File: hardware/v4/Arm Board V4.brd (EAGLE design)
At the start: 108 x 50.8 mm, 29 parts, among them P1 STELLARIS-LAUNCHPADSTELLARIS-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, U1 SN74LS241DW, U2 XBEE-1B3

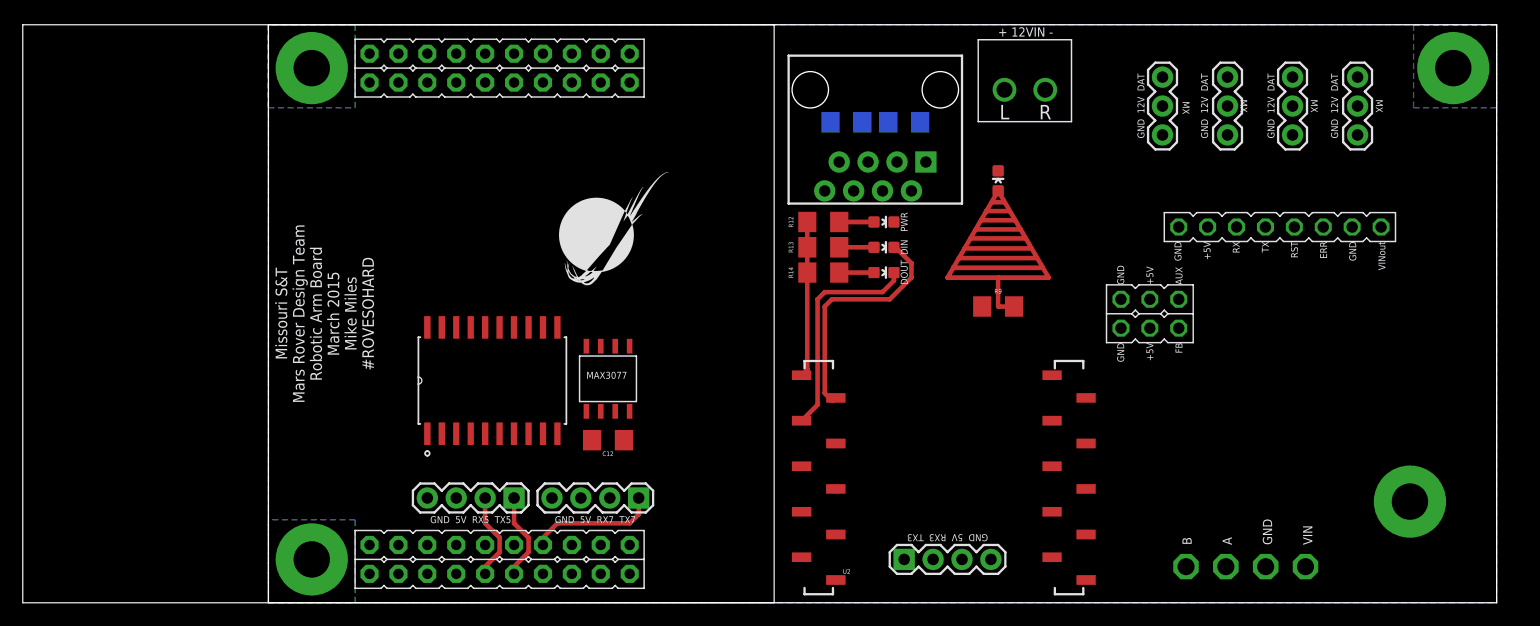
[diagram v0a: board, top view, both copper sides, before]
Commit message: reworking arm board
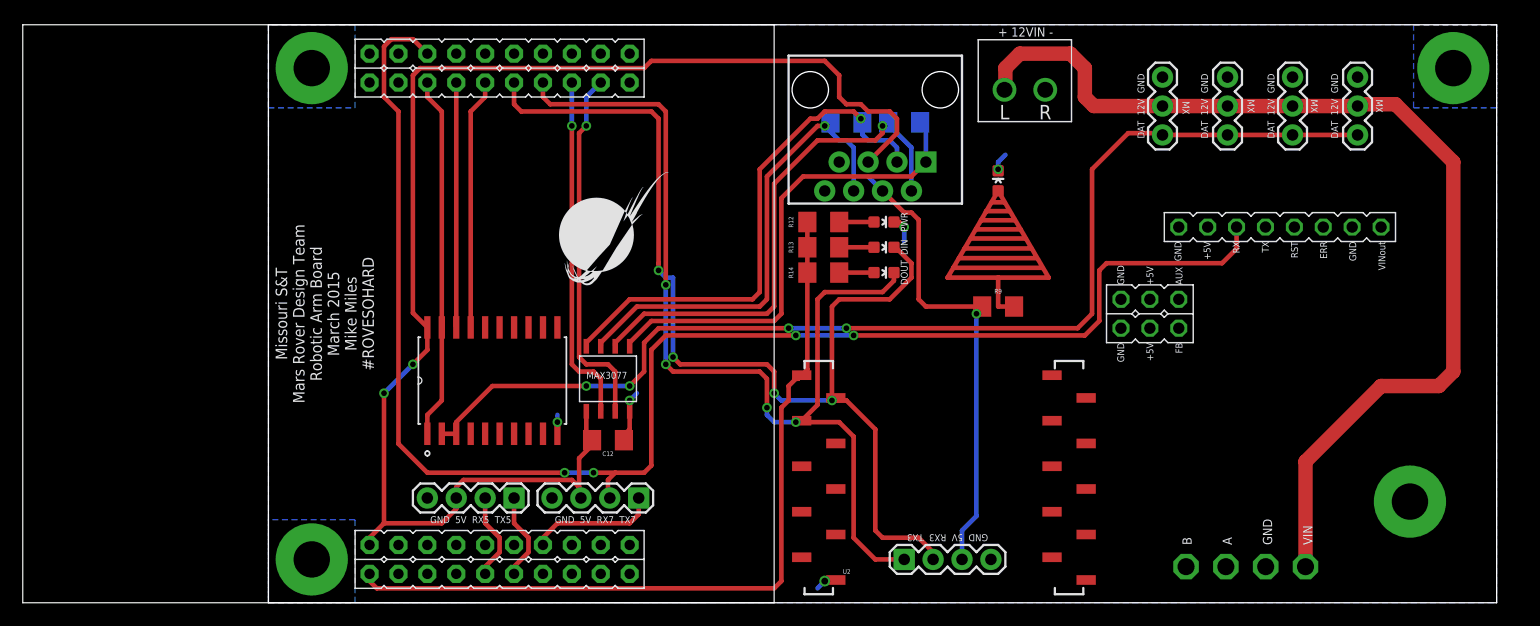
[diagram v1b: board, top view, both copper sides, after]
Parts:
- R9: value 1.5k -> 330
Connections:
- removed net 14.8V: JP10.2, JP11.2, JP12.2, JP9.2
- removed net VIN: R9.2
- net +12V: now also JP10.2, JP11.2, JP12.2, JP9.2
- net +5V: now also R9.2
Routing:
- net +5V: track 0.00 -> 165.3 mm, vias 0 -> 3
- net RX_7: track 0.00 -> 135.9 mm, vias 0 -> 4
- net DDATA_1: track 0.00 -> 101.0 mm, vias 0 -> 4
- net +12V: track 0.00 -> 91.3 mm
- net RX_3: track 21.0 -> 93.8 mm, vias 0 -> 4
- net TX_3: track 19.4 -> 89.4 mm, vias 0 -> 4
- net +3V3: track 13.7 -> 70.0 mm
- net N$1: track 0.00 -> 45.9 mm, vias 0 -> 1
- net N$3: track 0.00 -> 45.7 mm, vias 0 -> 1
- net N$5: track 0.00 -> 42.6 mm
- net N$2: track 0.00 -> 42.1 mm, vias 0 -> 1
- net TX_2: track 0.00 -> 32.1 mm, vias 0 -> 1
- net DC_1: track 0.00 -> 31.9 mm
- net RX_2: track 0.00 -> 30.7 mm, vias 0 -> 1
- net TX_1: track 0.00 -> 22.0 mm
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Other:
- board text added: "DAT 12V GND"
- board text removed: "GND 12V DAT"

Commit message: reworking arm board
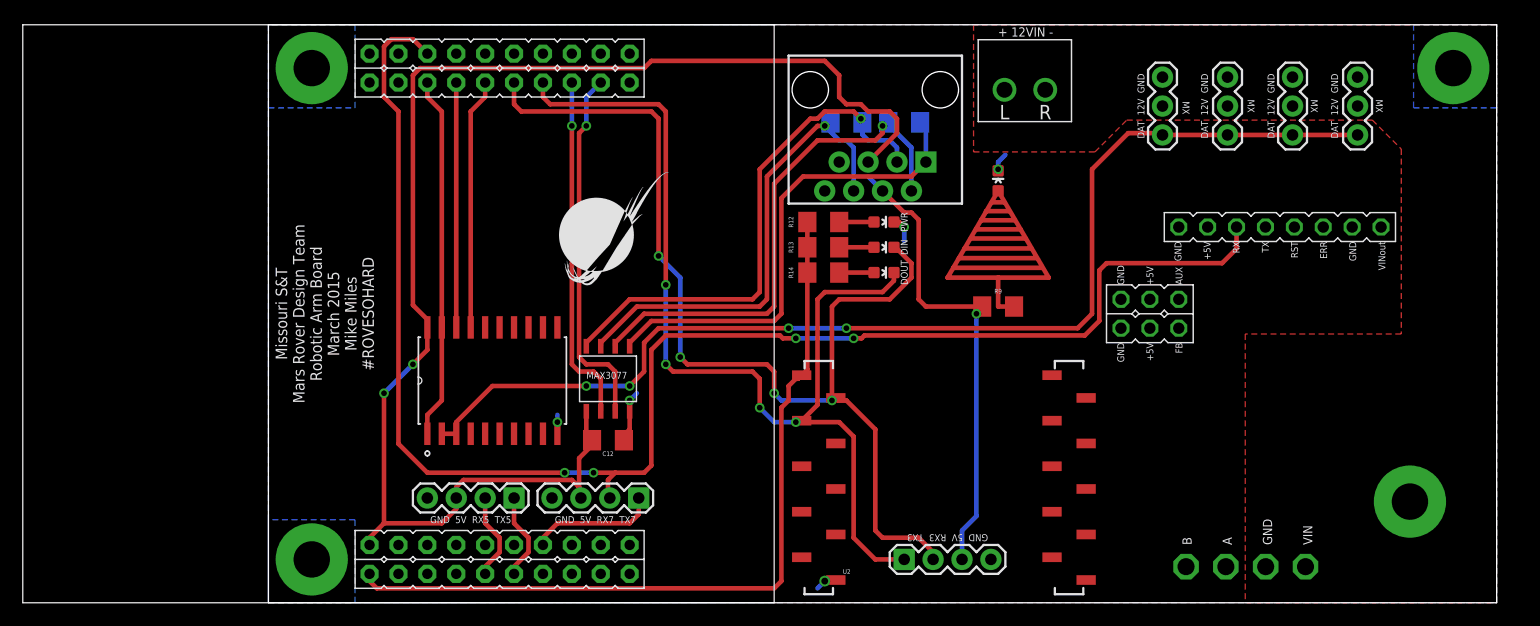
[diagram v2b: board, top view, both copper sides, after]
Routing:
- net +12V: track 91.3 -> 0.00 mm
- net RX_3: track 93.8 -> 93.0 mm
- added copper zone on layer 1, net +12V
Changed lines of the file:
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@@
 <setting verticaltext="up"/>
 </settings>
-<grid distance="0.05" unitdist="inch" unit="inch" style="lines" multiple="1" display="no" altdistance="0.025" altunitdist="inch" altunit="inch"/>
+<grid distance="0.01" unitdist="inch" unit="inch" style="lines" multiple="1" display="no" altdistance="0.0025" altunitdist="inch" altunit="inch"/>
 <layers>
 <layer number="1" name="Top" color="4" fill="1" visible="yes" active="yes"/>
@@
 <wire x1="33.02" y1="46.99" x2="13.335" y2="46.99" width="0.4064" layer="1"/>
 <wire x1="13.335" y1="46.99" x2="12.7" y2="46.355" width="0.4064" layer="1"/>
-<wire x1="12.7" y1="46.355" x2="12.7" y2="25.46985" width="0.4064" layer="1"/>
-<wire x1="12.7" y1="25.46985" x2="13.97" y2="24.19985" width="0.4064" layer="1"/>
 <wire x1="62.735" y1="26.035" x2="62.735" y2="25.905" width="0.4064" layer="1"/>
 <wire x1="62.735" y1="25.905" x2="62.23" y2="25.4" width="0.4064" layer="1"/>
@@
 <wire x1="62.23" y1="7.62" x2="60.96" y2="6.35" width="0.4064" layer="16"/>
 <wire x1="60.96" y1="6.35" x2="60.96" y2="3.81" width="0.4064" layer="16"/>
+<wire x1="13.97" y1="24.19985" x2="13.97" y2="24.892" width="0.4064" layer="1"/>
+<wire x1="13.97" y1="24.892" x2="12.7" y2="26.162" width="0.4064" layer="1"/>
+<wire x1="12.7" y1="26.162" x2="12.7" y2="46.355" width="0.4064" layer="1"/>
 <wire x1="52.705" y1="38.735" x2="52.705" y2="37.465" width="0" layer="19" extent="16-16"/>
 </signal>
@@
 <contactref element="U$7" pad="L"/>
 <contactref element="U$1" pad="VIN"/>
-<wire x1="91.149478125" y1="3.171971875" x2="91.149478125" y2="12.409478125" width="1.27" layer="1"/>
-<wire x1="91.149478125" y1="12.409478125" x2="97.79" y2="19.05" width="1.27" layer="1"/>
 <contactref element="JP9" pad="2"/>
 <contactref element="JP10" pad="2"/>
 <contactref element="JP11" pad="2"/>
 <contactref element="JP12" pad="2"/>
-<wire x1="97.79" y1="19.05" x2="102.87" y2="19.05" width="1.27" layer="1"/>
-<wire x1="102.87" y1="19.05" x2="104.14" y2="20.32" width="1.27" layer="1"/>
-<wire x1="104.14" y1="20.32" x2="104.14" y2="38.735" width="1.27" layer="1"/>
-<wire x1="104.14" y1="38.735" x2="99.06" y2="43.815" width="1.27" layer="1"/>
-<wire x1="99.06" y1="43.815" x2="95.885" y2="43.815" width="1.27" layer="1"/>
-<wire x1="95.885" y1="43.815" x2="95.72625" y2="43.65625" width="1.27" layer="1"/>
-<wire x1="95.72625" y1="43.65625" x2="90.01125" y2="43.65625" width="1.27" layer="1"/>
-<wire x1="90.01125" y1="43.65625" x2="84.29625" y2="43.65625" width="1.27" layer="1"/>
-<wire x1="84.29625" y1="43.65625" x2="78.58125" y2="43.65625" width="1.27" layer="1"/>
-<wire x1="78.58125" y1="43.65625" x2="72.54875" y2="43.65625" width="1.27" layer="1"/>
-<wire x1="72.54875" y1="43.65625" x2="71.755" y2="44.45" width="1.27" layer="1"/>
-<wire x1="71.755" y1="44.45" x2="71.755" y2="46.99" width="1.27" layer="1"/>
-<wire x1="71.755" y1="46.99" x2="70.485" y2="48.26" width="1.27" layer="1"/>
-<wire x1="70.485" y1="48.26" x2="66.04" y2="48.26" width="1.27" layer="1"/>
-<wire x1="66.04" y1="48.26" x2="64.77" y2="46.99" width="1.27" layer="1"/>
-<wire x1="64.77" y1="46.99" x2="64.77" y2="45.1605" width="1.27" layer="1"/>
-<wire x1="64.77" y1="45.1605" x2="64.6945" y2="45.085" width="1.27" layer="1"/>
+<polygon width="0.4064" layer="1">
+<vertex x="107.95" y="0"/>
+<vertex x="107.95" y="50.8"/>
+<vertex x="61.976" y="50.8"/>
+<vertex x="61.976" y="39.624"/>
+<vertex x="72.644" y="39.624"/>
+<vertex x="75.438" y="42.418"/>
+<vertex x="97.028" y="42.418"/>
+<vertex x="99.568" y="39.878"/>
+<vertex x="99.568" y="23.622"/>
+<vertex x="85.852" y="23.622"/>
+<vertex x="85.852" y="0"/>
+</polygon>
 </signal>
 <signal name="RST">
@@
 <wire x1="50.8" y1="17.78" x2="50.09" y2="17.78" width="0.4064" layer="1"/>
 <wire x1="50.09" y1="17.78" x2="49.87" y2="18" width="0.4064" layer="1"/>
-<wire x1="35.56" y1="28.575" x2="35.56" y2="21.59" width="0.4064" layer="16"/>
-<via x="35.56" y="21.59" extent="1-16" drill="0.5"/>
-<wire x1="35.56" y1="21.59" x2="36.195" y2="20.955" width="0.4064" layer="1"/>
-<wire x1="36.195" y1="20.955" x2="43.815" y2="20.955" width="0.4064" layer="1"/>
+<via x="36.195" y="21.59" extent="1-16" drill="0.5"/>
+<wire x1="36.195" y1="21.59" x2="36.83" y2="20.955" width="0.4064" layer="1"/>
+<wire x1="36.83" y1="20.955" x2="43.815" y2="20.955" width="0.4064" layer="1"/>
 <wire x1="43.815" y1="20.955" x2="44.45" y2="20.32" width="0.4064" layer="1"/>
 <wire x1="44.45" y1="20.32" x2="44.45" y2="18.415" width="0.4064" layer="1"/>
@@
 <wire x1="22.225" y1="43.18" x2="33.655" y2="43.18" width="0.4064" layer="1"/>
 <wire x1="33.655" y1="43.18" x2="34.29" y2="42.545" width="0.4064" layer="1"/>
-<wire x1="34.29" y1="42.545" x2="34.29" y2="29.845" width="0.4064" layer="1"/>
-<wire x1="35.56" y1="28.575" x2="34.925" y2="28.575" width="0.4064" layer="16"/>
-<wire x1="34.925" y1="28.575" x2="34.29" y2="29.21" width="0.4064" layer="16"/>
-<via x="34.29" y="29.21" extent="1-16" drill="0.5"/>
-<wire x1="34.29" y1="29.21" x2="34.29" y2="29.845" width="0.4064" layer="1"/>
+<wire x1="34.29" y1="42.545" x2="34.29" y2="30.48" width="0.4064" layer="1"/>
+<via x="34.29" y="30.48" extent="1-16" drill="0.5"/>
+<wire x1="34.29" y1="30.48" x2="36.195" y2="28.575" width="0.4064" layer="16"/>
+<wire x1="36.195" y1="28.575" x2="36.195" y2="21.59" width="0.4064" layer="16"/>
 </signal>
 <signal name="TX_3">
@@
 <via x="34.925" y="27.94" extent="1-16" drill="0.5"/>
 <wire x1="34.925" y1="27.94" x2="34.925" y2="20.955" width="0.4064" layer="16"/>
-<via x="43.815" y="17.145" extent="1-16" drill="0.5"/>
-<wire x1="43.815" y1="17.145" x2="43.815" y2="16.51" width="0.4064" layer="16"/>
-<wire x1="43.815" y1="16.51" x2="44.45" y2="15.875" width="0.4064" layer="16"/>
 <wire x1="44.45" y1="15.875" x2="46.355" y2="15.875" width="0.4064" layer="16"/>
 <via x="46.355" y="15.875" extent="1-16" drill="0.5"/>
@@
 <via x="34.925" y="20.955" extent="1-16" drill="0.5"/>
 <wire x1="34.925" y1="20.955" x2="35.56" y2="20.32" width="0.4064" layer="1"/>
-<wire x1="35.56" y1="20.32" x2="43.18" y2="20.32" width="0.4064" layer="1"/>
-<wire x1="43.18" y1="20.32" x2="43.815" y2="19.685" width="0.4064" layer="1"/>
-<wire x1="43.815" y1="19.685" x2="43.815" y2="17.145" width="0.4064" layer="1"/>
 <wire x1="24.13" y1="45.72" x2="24.13" y2="44.45" width="0.4064" layer="1"/>
 <wire x1="24.13" y1="44.45" x2="24.765" y2="43.815" width="0.4064" layer="1"/>
@@
 <wire x1="34.29" y1="43.815" x2="34.925" y2="43.18" width="0.4064" layer="1"/>
 <wire x1="34.925" y1="43.18" x2="34.925" y2="27.94" width="0.4064" layer="1"/>
+<wire x1="35.56" y1="20.32" x2="42.545" y2="20.32" width="0.4064" layer="1"/>
+<wire x1="42.545" y1="20.32" x2="43.18" y2="19.685" width="0.4064" layer="1"/>
+<wire x1="43.18" y1="19.685" x2="43.18" y2="17.145" width="0.4064" layer="1"/>
+<via x="43.18" y="17.145" extent="1-16" drill="0.5"/>
+<wire x1="43.18" y1="17.145" x2="44.45" y2="15.875" width="0.4064" layer="16"/>
 </signal>
 <signal name="RX_1">
@@
 <contactref element="P1" pad="PC5"/>
 <contactref element="U1" pad="17"/>
-<wire x1="17.78" y1="24.19985" x2="17.78" y2="43.18" width="0.4064" layer="1"/>
 <wire x1="17.78" y1="43.18" x2="19.05" y2="44.45" width="0.4064" layer="1"/>
 <wire x1="19.05" y1="44.45" x2="19.05" y2="45.72" width="0.4064" layer="1"/>
+<wire x1="17.78" y1="24.19985" x2="17.78" y2="43.18" width="0.4064" layer="1"/>
 </signal>
 <signal name="RX_5">
@@
 <wire x1="73.025" y1="29.21" x2="73.025" y2="24.765" width="0.4064" layer="1"/>
 <wire x1="73.025" y1="24.765" x2="71.755" y2="23.495" width="0.4064" layer="1"/>
-<wire x1="71.755" y1="23.495" x2="51.435" y2="23.495" width="0.4064" layer="1"/>
-<via x="51.435" y="23.495" extent="1-16" drill="0.5"/>
+<wire x1="71.755" y1="23.495" x2="52.3875" y2="23.495" width="0.4064" layer="1"/>
+<wire x1="52.3875" y1="23.495" x2="52.1335" y2="23.241" width="0.4064" layer="1"/>
+<wire x1="52.1335" y1="23.241" x2="51.435" y2="23.241" width="0.4064" layer="1"/>
+<via x="51.435" y="23.241" extent="1-16" drill="0.5"/>
 <wire x1="34.925" y1="23.495" x2="33.655" y2="22.225" width="0.4064" layer="1"/>
 <wire x1="33.655" y1="22.225" x2="33.655" y2="12.065" width="0.4064" layer="1"/>
@@
 <via x="28.575" y="11.43" extent="1-16" drill="0.5"/>
 <wire x1="28.575" y1="11.43" x2="30.48" y2="11.43" width="0.4064" layer="1"/>
-<wire x1="34.925" y1="23.495" x2="46.355" y2="23.495" width="0.4064" layer="1"/>
-<via x="46.355" y="23.495" extent="1-16" drill="0.5"/>
-<wire x1="46.355" y1="23.495" x2="51.435" y2="23.495" width="0.4064" layer="16"/>
+<wire x1="34.925" y1="23.495" x2="44.958" y2="23.495" width="0.4064" layer="1"/>
+<wire x1="44.958" y1="23.495" x2="45.212" y2="23.241" width="0.4064" layer="1"/>
+<wire x1="45.212" y1="23.241" x2="46.355" y2="23.241" width="0.4064" layer="1"/>
+<via x="46.355" y="23.241" extent="1-16" drill="0.5"/>
+<wire x1="46.355" y1="23.241" x2="51.435" y2="23.241" width="0.4064" layer="16"/>
 <wire x1="11.43" y1="43.18" x2="10.16" y2="44.45" width="0.4064" layer="1"/>
 <wire x1="10.16" y1="44.45" x2="10.16" y2="48.895" width="0.4064" layer="1"/>

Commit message: Updated stuffs
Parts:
- moved LED5 9.72 mm to (69.5, 29.0)
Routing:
- net N$14: track 30.5 -> 4.78 mm
- net N$13: track 7.78 -> 0.00 mm
- net N$15: track 6.78 -> 0.00 mm
- net N$16: track 5.83 -> 0.00 mm
- net N$20: track 4.75 -> 0.00 mm
- net N$23: track 3.93 -> 0.00 mm
- net N$24: track 2.93 -> 0.00 mm
- net N$25: track 2.03 -> 0.00 mm
- net GND: track 13.5 -> 12.0 mm
- net N$26: track 1.08 -> 0.00 mm

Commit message: still reworking arm board
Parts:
- removed LED5: RED, SparkFun-LED:LED-0603
- removed R9: 330, SparkFun-Passives:1206
- added D1: RED, SparkFun-LED:LED-0603
- moved C12 26.0 mm to (34.9, 39.8), turned to 270 degrees
- moved U$4 22.7 mm to (40.5, 39.8), turned to 270 degrees
- moved R12 9.32 mm to (45.8, 24.6), turned to 270 degrees
- moved LED1 9.02 mm to (45.8, 30.0), turned to 0 degrees
- moved R13 6.65 mm to (48.0, 24.6), turned to 90 degrees
- moved LED2 6.23 mm to (48.0, 30.0), turned to 0 degrees
- moved R14 4.62 mm to (50.2, 24.6), turned to 90 degrees
- moved LED3 3.99 mm to (50.2, 30.0), turned to 0 degrees
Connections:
- removed net N$14: LED5.A, R9.1
- new net DDATA_OUT: D1.A, U1.2, U1.3
- net +5V: no longer R9.2
- net DDATA_1: now also D1.C; no longer U1.2, U1.3
- net GND: no longer LED5.C
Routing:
- net DDATA_OUT: track 0.00 -> 87.2 mm, vias 0 -> 2
- net DDATA_1: track 101.0 -> 19.6 mm, vias 4 -> 0
- net N$3: track 45.7 -> 14.9 mm
- net N$2: track 42.1 -> 14.8 mm
- net +5V: track 165.3 -> 186.8 mm, vias 3 -> 1
- net N$1: track 45.9 -> 26.2 mm, vias 1 -> 2
- net N$5: track 42.6 -> 23.9 mm
- net TX_2: track 32.1 -> 17.7 mm, vias 1 -> 0
- net RX_2: track 30.7 -> 18.3 mm, vias 1 -> 0
- net RX_3: track 93.0 -> 80.9 mm, vias 4 -> 1
- net TX_3: track 89.0 -> 77.5 mm, vias 4 -> 3
- net +3V3: track 70.0 -> 64.8 mm
- net N$14: track 4.78 -> 0.00 mm
- net GND: track 12.0 -> 10.5 mm, vias 5 -> 4
- net RX_7: track 136.1 -> 135.3 mm, vias 4 -> 2
- added copper zone on layer 16, net N$10
